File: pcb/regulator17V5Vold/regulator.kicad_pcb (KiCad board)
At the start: 2 copper layers, 10 x 16.5 mm, 8 parts, among them J1 Conn_01x05_Socket, J2 Conn_01x05_Socket, J3 Conn_01x02, U1 TPS82130

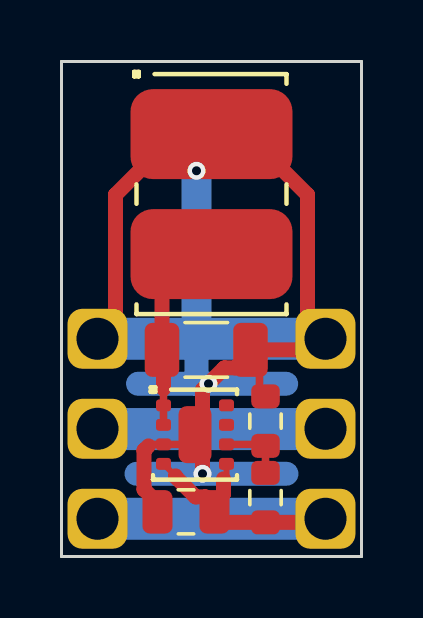
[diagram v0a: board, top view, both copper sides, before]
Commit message: Add receiver for IKEA Metod cupboard
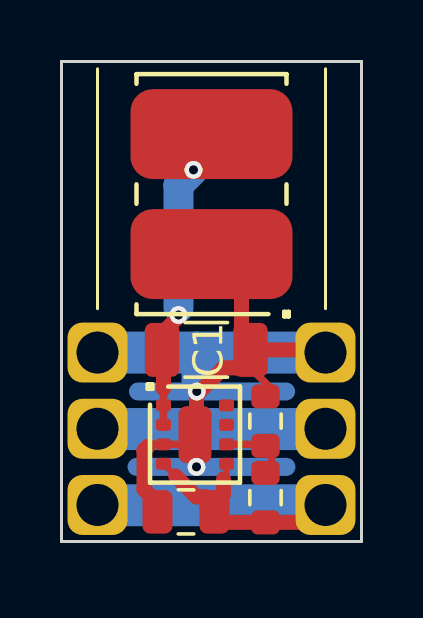
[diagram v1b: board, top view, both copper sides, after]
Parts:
- J1, J2: footprint local:SolderHoles3pin10mm -> local:Holes
- turned J3 to 90 degrees
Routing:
- net GND: track 57.3 -> 35.6 mm, vias 3 -> 2
- net +15V: track 5.51 -> 8.63 mm, vias 0 -> 2
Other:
- board size 10 x 16.5 mm -> 10 x 16 mm

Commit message: Use ISL3280E
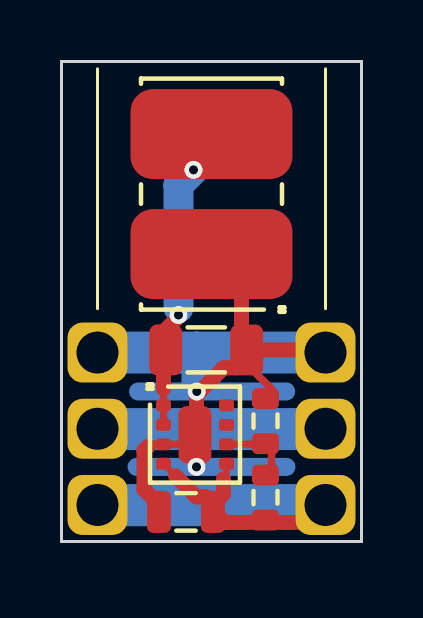
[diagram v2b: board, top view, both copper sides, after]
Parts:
- C1: footprint Capacitor_SMD:C_1206_3216Metric -> local:1206
- C2: footprint Capacitor_SMD:C_0805_2012Metric -> local:0805
- R1, R2: footprint Resistor_SMD:R_0603_1608Metric -> local:0603
- turned U1 to 0 degrees
